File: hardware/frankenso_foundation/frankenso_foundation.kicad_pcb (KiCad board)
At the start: 2 copper layers, 5 parts, among them P99 0176122-06

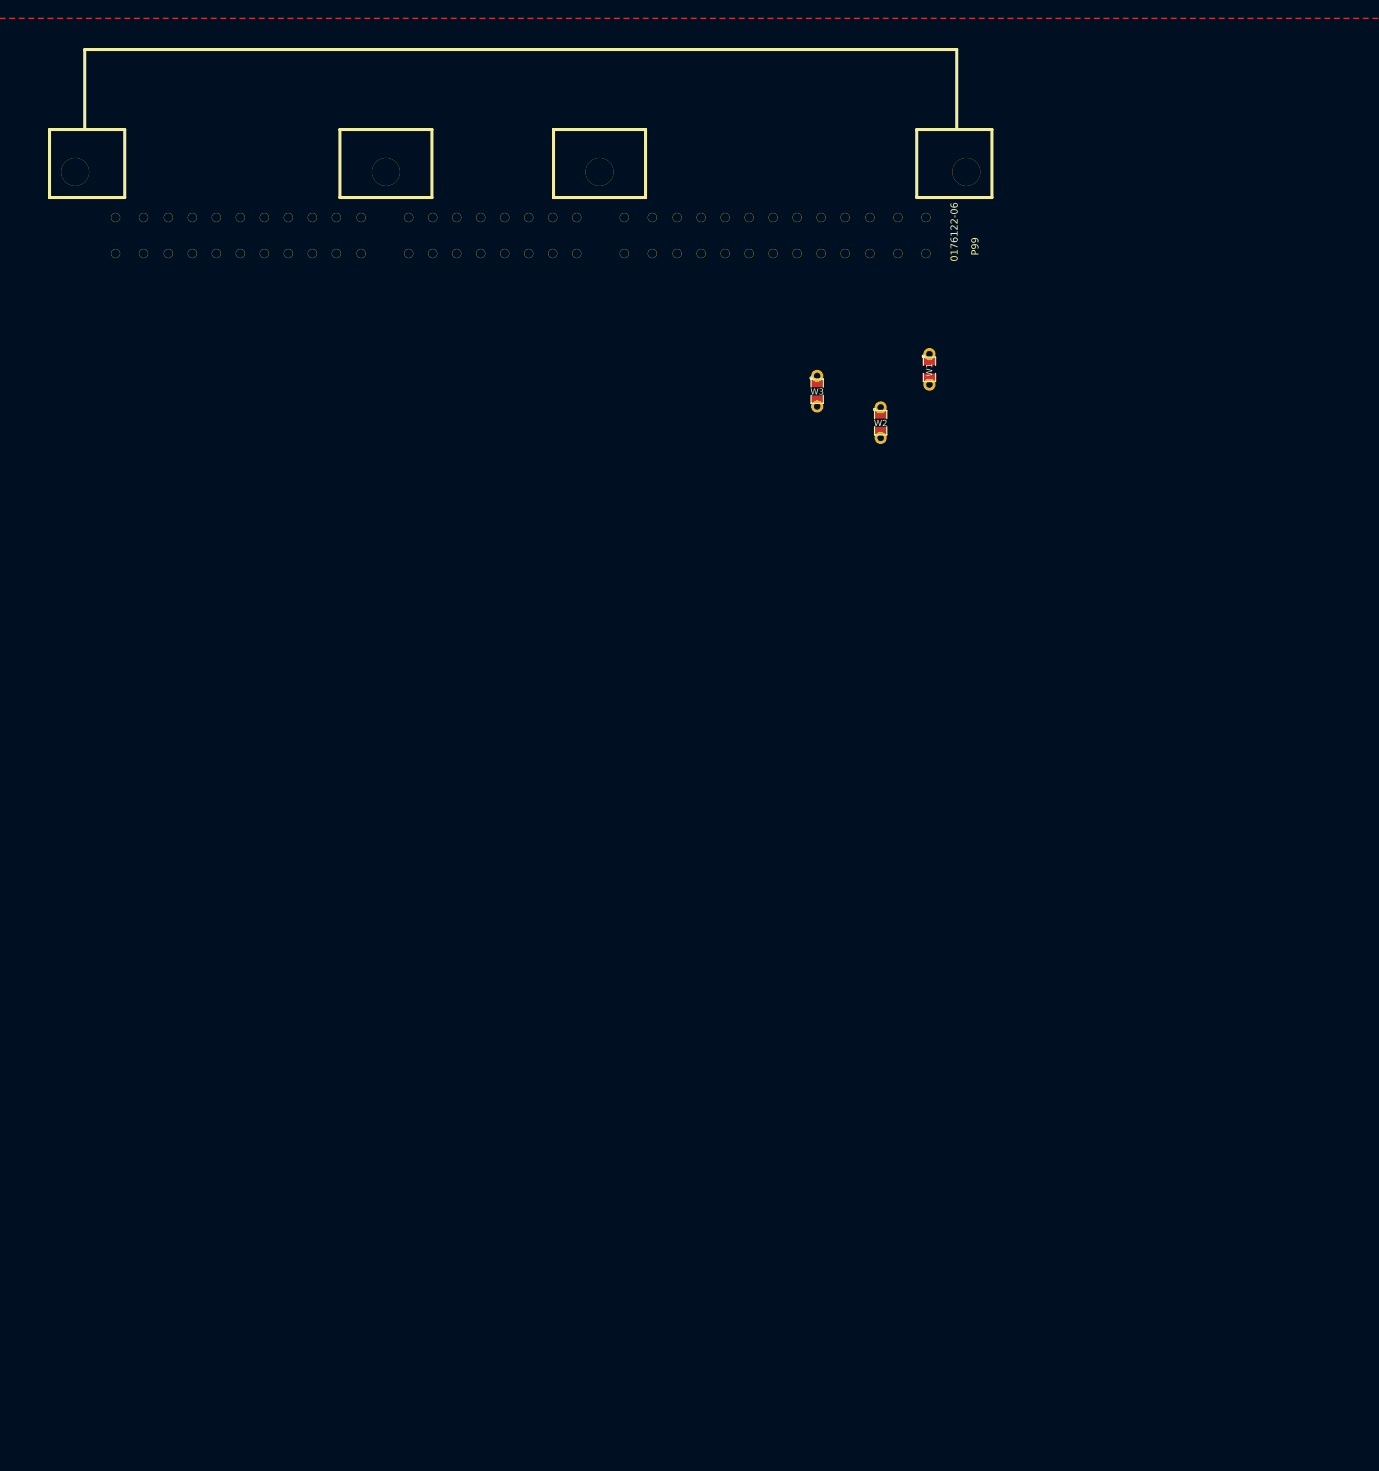
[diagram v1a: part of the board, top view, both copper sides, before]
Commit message: 
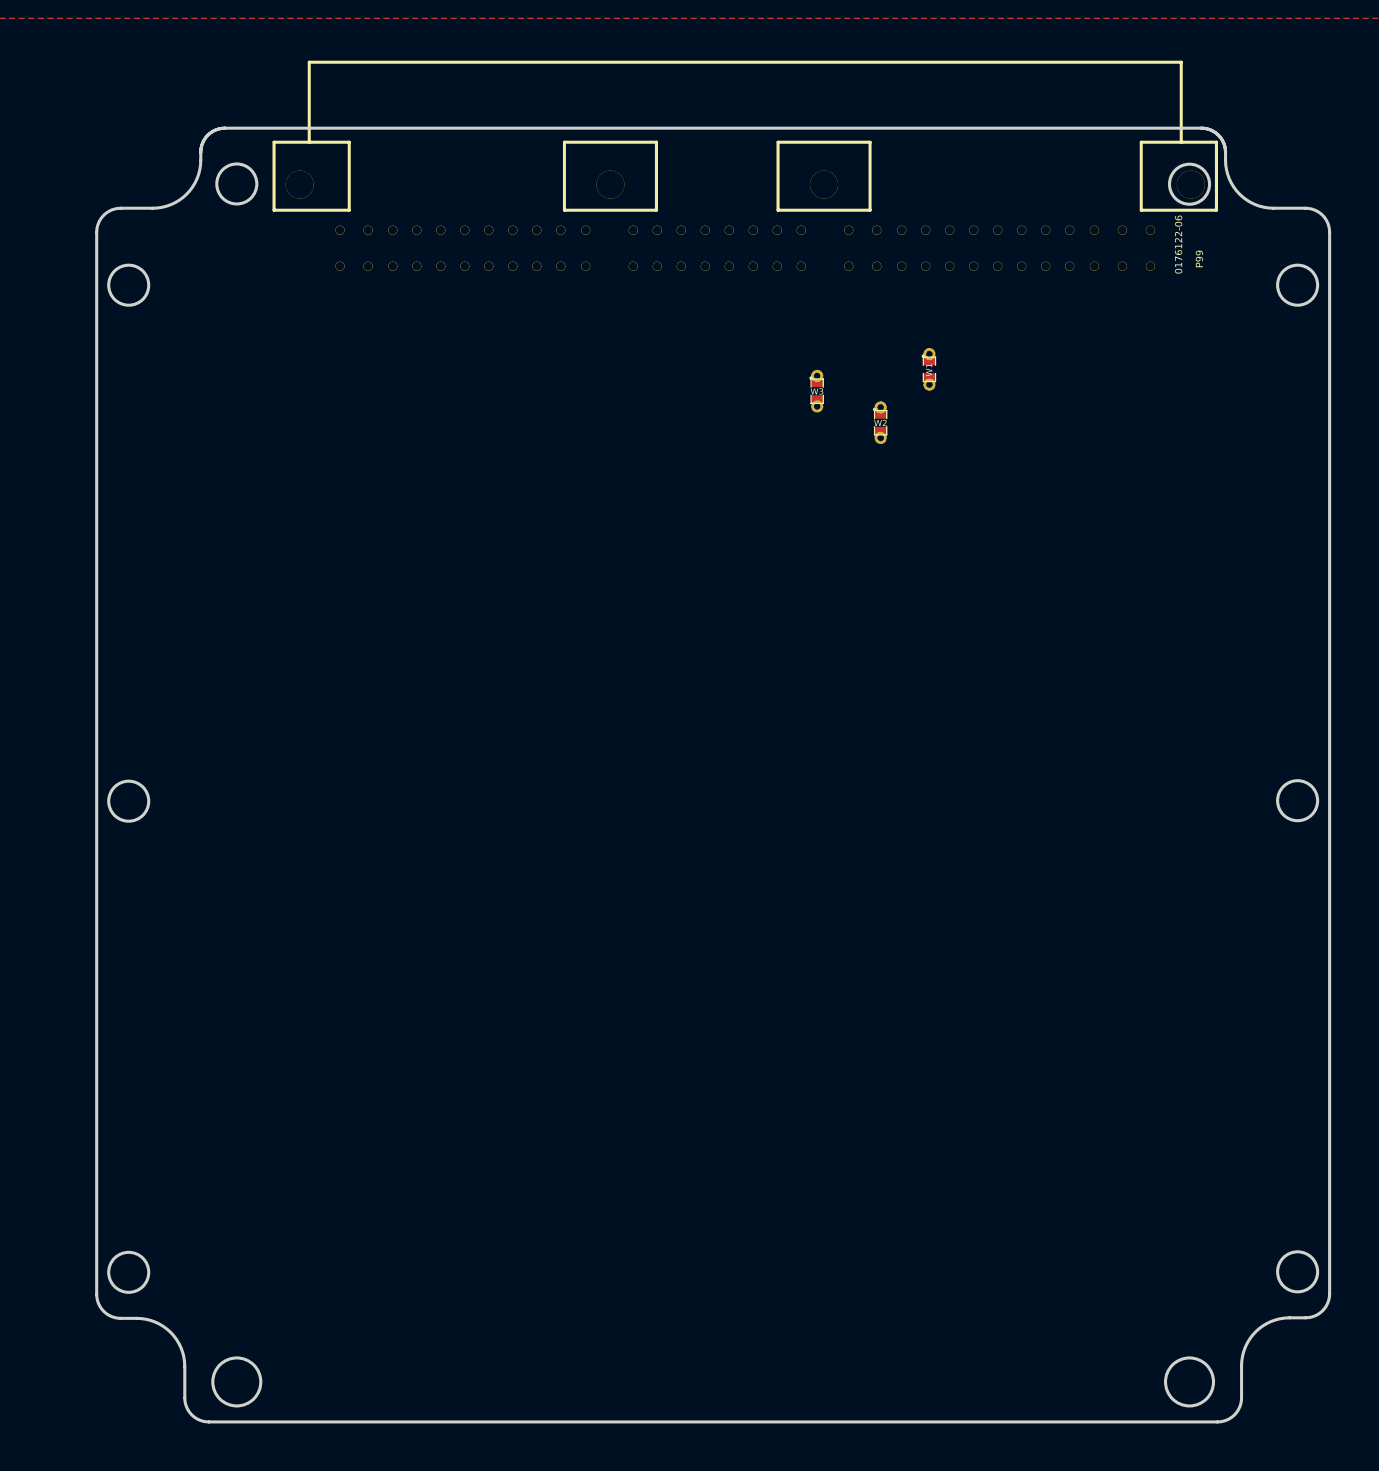
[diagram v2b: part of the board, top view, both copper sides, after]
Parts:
- moved P99 28.1 mm to (250.6, 110.0)
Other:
- board outline added: 154.1 x 161.7 mm
- net class Default: clearance 0.2032 -> 0.254
- rule pad_to_mask_clearance: 0 -> 0.2
- rule trace_clearance: 0.2032 -> 0.254
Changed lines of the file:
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@@
     (links 12)
     (no_connects 12)
-    (area 0 0 0 0)
+    (area 92 76 293.000001 271.000001)
     (thickness 1.6)
-    (drawings 13)
+    (drawings 49)
     (tracks 0)
     (zones 0)
@@
   (setup
     (last_trace_width 0.254)
-    (trace_clearance 0.2032)
-    (zone_clearance 0.254)
+    (trace_clearance 0.254)
+    (zone_clearance 0.381)
     (zone_45_only no)
     (trace_min 0.254)
-    (segment_width 0.2)
-    (edge_width 0.1)
+    (segment_width 0.3)
+    (edge_width 0.381)
     (via_size 0.889)
     (via_drill 0.635)
@@
     (uvia_min_size 0.508)
     (uvia_min_drill 0.127)
-    (pcb_text_width 0.3)
-    (pcb_text_size 1.5 1.5)
-    (mod_edge_width 0.15)
-    (mod_text_size 1 1)
-    (mod_text_width 0.15)
+    (pcb_text_width 0.3048)
+    (pcb_text_size 1.524 2.032)
+    (mod_edge_width 0.381)
+    (mod_text_size 1.524 1.524)
+    (mod_text_width 0.3048)
     (pad_size 1.524 1.524)
-    (pad_drill 1.016)
-    (pad_to_mask_clearance 0)
+    (pad_drill 0.508)
+    (pad_to_mask_clearance 0.2)
     (aux_axis_origin 0 0)
-    (visible_elements 7FFFFFBF)
+    (visible_elements 7FFFFFFF)
     (pcbplotparams
-      (layerselection 318537729)
+      (layerselection 3178497)
       (usegerberextensions true)
       (excludeedgelayer true)
-      (linewidth 0.150000)
+      (linewidth 0.100000)
       (plotframeref false)
       (viasonmask false)
@@
       (outputformat 1)
       (mirror false)
-      (drillshape 0)
+      (drillshape 1)
       (scaleselection 1)
-      (outputdirectory gerber))
+      (outputdirectory ""))
   )
   (net 0 "")
@@
   (net 5 N-000003)
   (net 6 N-000004)
-  (net_class Default "This is the default net class."
-    (clearance 0.2032)
+  (net_class Default "Это класс цепей по умолчанию."
+    (clearance 0.254)
     (trace_width 0.254)
     (via_dia 0.889)
@@
   )
   (module 176122-6 (layer F.Cu)
-    (at 222.504 108.3945)
+    (at 250.571 109.982)
     (fp_text reference P99 (at -2.10058 -0.89916 270) (layer F.SilkS)
       (effects (font (size 0.889 0.889) (thickness 0.22352)))
@@
   (gr_line (start 127 238.76) (end 129.54 238.76) (angle 90) (layer Cmts.User) (width 0.2))
   (gr_line (start 127 177.8) (end 127 238.76) (angle 90) (layer Cmts.User) (width 0.2))
+  (gr_circle (center 260.714 112.35478) (end 260.714 114.85668) (layer Edge.Cuts) (width 0.381))
+  (gr_circle (center 114.60304 112.35478) (end 114.60304 114.85668) (layer Edge.Cuts) (width 0.381))
+  (gr_arc (start 248.70488 95.72972) (end 251.70716 95.72972) (angle -90) (layer Edge.Cuts) (width 0.381))
+  (gr_circle (center 247.20374 249.44772) (end 247.20374 252.44772) (layer Edge.Cuts) (width 0.381))
+  (gr_arc (start 126.61216 95.72972) (end 126.61216 92.72744) (angle -90) (layer Edge.Cuts) (width 0.381))
+  (gr_circle (center 128.1133 249.44772) (end 128.1133 252.44772) (layer Edge.Cuts) (width 0.381))
+  (gr_line (start 250.70488 254.44772) (end 124.61216 254.44772) (angle 90) (layer Edge.Cuts) (width 0.381))
+  (gr_circle (center 247.20374 99.73276) (end 247.20374 102.23466) (layer Edge.Cuts) (width 0.381))
+  (gr_circle (center 128.1133 99.70228) (end 128.1133 102.20418) (layer Edge.Cuts) (width 0.381))
+  (gr_circle (center 260.714 176.79128) (end 260.714 179.29318) (layer Edge.Cuts) (width 0.381))
+  (gr_circle (center 260.714 235.68404) (end 260.714 238.18594) (layer Edge.Cuts) (width 0.381))
+  (gr_circle (center 114.60304 176.85478) (end 114.60304 179.35668) (layer Edge.Cuts) (width 0.381))
+  (gr_circle (center 114.60304 235.74754) (end 114.60304 238.24944) (layer Edge.Cuts) (width 0.381))
+  (gr_line (start 123.60988 95.72972) (end 123.60988 96.73048) (angle 90) (layer Edge.Cuts) (width 0.381))
+  (gr_line (start 117.60532 102.73504) (end 113.60228 102.73504) (angle 90) (layer Edge.Cuts) (width 0.381))
+  (gr_arc (start 117.60532 96.73048) (end 117.60532 102.73504) (angle -90) (layer Edge.Cuts) (width 0.381))
+  (gr_line (start 126.61216 92.72744) (end 248.70488 92.72744) (angle 90) (layer Edge.Cuts) (width 0.381))
+  (gr_line (start 251.70716 95.72972) (end 251.70716 96.73048) (angle 90) (layer Edge.Cuts) (width 0.381))
+  (gr_line (start 257.71172 102.73504) (end 261.71476 102.73504) (angle 90) (layer Edge.Cuts) (width 0.381))
+  (gr_arc (start 257.71172 96.73048) (end 251.70716 96.73048) (angle -90) (layer Edge.Cuts) (width 0.381))
+  (gr_arc (start 248.70488 95.72972) (end 251.70716 95.72972) (angle -90) (layer Edge.Cuts) (width 0.381))
+  (gr_arc (start 126.61216 95.72972) (end 126.61216 92.72744) (angle -90) (layer Edge.Cuts) (width 0.381))
+  (gr_line (start 253.70716 251.44544) (end 253.70716 247.43732) (angle 90) (layer Edge.Cuts) (width 0.381))
+  (gr_line (start 259.71172 241.43276) (end 261.71476 241.43276) (angle 90) (layer Edge.Cuts) (width 0.381))
+  (gr_line (start 115.60532 241.50134) (end 113.60228 241.50134) (angle 90) (layer Edge.Cuts) (width 0.381))
+  (gr_arc (start 259.71172 247.43732) (end 259.71172 241.43276) (angle -90) (layer Edge.Cuts) (width 0.381))
+  (gr_arc (start 115.60532 247.5059) (end 121.60988 247.5059) (angle -90) (layer Edge.Cuts) (width 0.381))
+  (gr_line (start 121.60988 247.5059) (end 121.60988 251.44544) (angle 90) (layer Edge.Cuts) (width 0.381))
+  (gr_line (start 110.6 105.73732) (end 110.6 238.49906) (angle 90) (layer Edge.Cuts) (width 0.381))
+  (gr_line (start 264.71704 105.73732) (end 264.71704 238.43048) (angle 90) (layer Edge.Cuts) (width 0.381))
+  (gr_arc (start 261.71476 105.73732) (end 264.71704 105.73732) (angle -89.9) (layer Edge.Cuts) (width 0.381))
+  (gr_arc (start 261.71476 238.43048) (end 261.71476 241.43276) (angle -90) (layer Edge.Cuts) (width 0.381))
+  (gr_arc (start 250.70488 251.44544) (end 250.70488 254.44772) (angle -90) (layer Edge.Cuts) (width 0.381))
+  (gr_arc (start 124.61216 251.44544) (end 121.60988 251.44544) (angle -90) (layer Edge.Cuts) (width 0.381))
+  (gr_arc (start 113.60228 238.49906) (end 110.6 238.49906) (angle -89.9) (layer Edge.Cuts) (width 0.381))
+  (gr_arc (start 113.60228 105.73732) (end 113.60228 102.73504) (angle -90) (layer Edge.Cuts) (width 0.381))
   (zone (net -1) (net_name GND) (layer F.Cu) (hatch edge 0.508)
     (connect_pads (clearance 0.254))

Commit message: frankenso foundation progress
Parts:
- removed P_VOID3: CONN_8, pin_array_8x2
- added W10: TEST, SM0805_jumper, F.Cu at (151.8, 64.8)
- added W11: TEST, SM0805_jumper, F.Cu at (156.8, 71.1)
- added W12: TEST, SM0805_jumper, F.Cu at (154.9, 64.8)
- added W13: TEST, SM0805_jumper, F.Cu at (160.0, 71.1)
- added W14: TEST, SM0805_jumper, F.Cu at (158.1, 64.8)
- added W15: TEST, SM0805_jumper, F.Cu at (163.2, 71.1)
- added W16: TEST, SM0805_jumper, F.Cu at (161.3, 64.8)
- added W17: TEST, SM0805_jumper, F.Cu at (166.4, 71.1)
- added W18: TEST, SM0805_jumper, F.Cu at (164.5, 64.8)
- added W19: TEST, SM0805_jumper, F.Cu at (169.5, 71.1)
- added W20: TEST, SM0805_jumper, F.Cu at (167.6, 64.8)
- added W21: TEST, SM0805_jumper, F.Cu at (172.7, 71.1)
- added W22: TEST, SM0805_jumper, F.Cu at (170.8, 64.8)
- added W23: TEST, SM0805_jumper, F.Cu at (177.8, 71.1)
- added W24: TEST, SM0805_jumper, F.Cu at (175.9, 64.8)
- added W25: TEST, SM0805_jumper, F.Cu at (181.0, 71.1)
- added W26: TEST, SM0805_jumper, F.Cu at (179.1, 64.8)
- added W27: TEST, SM0805_jumper, F.Cu at (184.2, 71.1)
- added W28: TEST, SM0805_jumper, F.Cu at (182.2, 64.8)
- added W29: TEST, SM0805_jumper, F.Cu at (187.3, 71.1)
- added W30: TEST, SM0805_jumper, F.Cu at (185.4, 64.8)
- added W31: TEST, SM0805_jumper, F.Cu at (190.5, 71.1)
- added W32: TEST, SM0805_jumper, F.Cu at (188.6, 64.8)
- added W33: TEST, SM0805_jumper, F.Cu at (193.7, 71.1)
- added W34: TEST, SM0805_jumper, F.Cu at (191.8, 64.8)
- added W35: TEST, SM0805_jumper, F.Cu at (196.8, 71.1)
- added W36: TEST, SM0805_jumper, F.Cu at (194.9, 64.8)
- added W37: TEST, SM0805_jumper, F.Cu at (200.0, 71.1)
- added W38: TEST, SM0805_jumper, F.Cu at (198.1, 64.8)
- added W39: TEST, SM0805_jumper, F.Cu at (205.1, 71.1)
- added W4: TEST, SM0805_jumper, F.Cu at (142.2, 64.8)
- added W40: TEST, SM0805_jumper, F.Cu at (203.2, 64.8)
- added W41: TEST, SM0805_jumper, F.Cu at (208.3, 71.1)
- added W42: TEST, SM0805_jumper, F.Cu at (206.4, 64.8)
- added W43: TEST, SM0805_jumper, F.Cu at (211.5, 71.1)
- added W44: TEST, SM0805_jumper, F.Cu at (209.6, 64.8)
- added W45: TEST, SM0805_jumper, F.Cu at (214.6, 71.1)
- added W46: TEST, SM0805_jumper, F.Cu at (212.7, 64.8)
- added W47: TEST, SM0805_jumper, F.Cu at (217.8, 71.1)
- added W48: TEST, SM0805_jumper, F.Cu at (215.9, 64.8)
- added W49: TEST, SM0805_jumper, F.Cu at (221.0, 71.1)
- added W5: TEST, SM0805_jumper, F.Cu at (147.3, 71.1)
- added W50: TEST, SM0805_jumper, F.Cu at (219.1, 64.8)
- added W51: TEST, SM0805_jumper, F.Cu at (224.2, 71.1)
- added W52: TEST, SM0805_jumper, F.Cu at (222.2, 64.8)
- added W53: TEST, SM0805_jumper, F.Cu at (227.3, 71.1)
- added W54: TEST, SM0805_jumper, F.Cu at (225.4, 64.8)
- added W55: TEST, SM0805_jumper, F.Cu at (230.5, 71.1)
- added W56: TEST, SM0805_jumper, F.Cu at (228.6, 64.8)
- added W57: TEST, SM0805_jumper, F.Cu at (233.7, 71.1)
- added W58: TEST, SM0805_jumper, F.Cu at (231.8, 64.8)
- added W59: TEST, SM0805_jumper, F.Cu at (236.9, 71.1)
- added W6: TEST, SM0805_jumper, F.Cu at (145.4, 64.8)
- added W60: TEST, SM0805_jumper, F.Cu at (234.9, 64.8)
- added W61: TEST, SM0805_jumper, F.Cu at (240.0, 71.1)
- added W62: TEST, SM0805_jumper, F.Cu at (238.1, 64.8)
- added W63: TEST, SM0805_jumper, F.Cu at (243.2, 71.1)
- added W64: TEST, SM0805_jumper, F.Cu at (241.3, 64.8)
- added W7: TEST, SM0805_jumper, F.Cu at (150.5, 71.1)
- added W8: TEST, SM0805_jumper, F.Cu at (148.6, 64.8)
- added W9: TEST, SM0805_jumper, F.Cu at (153.7, 71.1)
- P99: value 0176122-06 -> 176122-6_2ND; footprint 176122-6 -> 176122-6_2nd
- moved W2 95.0 mm to (139.1, 64.8), turned to 90 degrees
- moved W1 90.1 mm to (141.0, 71.1), turned to 90 degrees
- moved W3 78.5 mm to (144.1, 71.1), turned to 90 degrees
- moved P99 50.5 mm to (250.8, 59.4)
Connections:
- P99 pad 1: N-000003 -> N-00000104
- P99 pad 10: (no net) -> N-00000108
- P99 pad 11: (no net) -> N-0000083
- P99 pad 12: (no net) -> N-00000102
- P99 pad 13: (no net) -> N-0000098
- P99 pad 14: (no net) -> N-0000094
- P99 pad 15: (no net) -> N-0000090
- P99 pad 16: (no net) -> N-0000086
- P99 pad 17: (no net) -> N-00000121
- P99 pad 18: (no net) -> N-00000117
- P99 pad 19: (no net) -> N-00000114
- P99 pad 2: N-000004 -> N-00000100
- P99 pad 20: (no net) -> N-00000110
- P99 pad 21: (no net) -> N-00000106
- P99 pad 22: (no net) -> N-0000081
- P99 pad 23: (no net) -> N-0000051
- P99 pad 24: (no net) -> N-0000049
- P99 pad 25: (no net) -> N-0000044
- P99 pad 26: (no net) -> N-0000040
- P99 pad 27: (no net) -> N-0000036
- P99 pad 28: (no net) -> N-0000032
- P99 pad 29: (no net) -> N-0000028
- P99 pad 3: N-000002 -> N-0000096
- P99 pad 30: (no net) -> N-0000046
- P99 pad 31: (no net) -> N-0000050
- P99 pad 32: (no net) -> N-0000048
- P99 pad 33: (no net) -> N-0000042
- P99 pad 34: (no net) -> N-0000038
- P99 pad 35: (no net) -> N-0000034
- P99 pad 36: (no net) -> N-0000030
- P99 pad 37: (no net) -> N-0000026
- P99 pad 38: (no net) -> N-0000045
- P99 pad 39: (no net) -> N-000003
- P99 pad 4: (no net) -> N-0000092
- P99 pad 40: (no net) -> N-0000024
- P99 pad 41: (no net) -> N-0000020
- P99 pad 42: (no net) -> N-0000016
- P99 pad 43: (no net) -> N-0000013
- P99 pad 44: (no net) -> N-000009
- P99 pad 45: (no net) -> N-0000079
- P99 pad 46: (no net) -> N-0000075
- P99 pad 47: (no net) -> N-0000071
- P99 pad 48: (no net) -> N-0000068
- P99 pad 49: (no net) -> N-0000059
- P99 pad 5: (no net) -> N-0000088
- P99 pad 50: (no net) -> N-0000058
- P99 pad 51: (no net) -> N-0000056
- P99 pad 52: (no net) -> N-000001
- P99 pad 53: (no net) -> N-0000022
- P99 pad 54: (no net) -> N-0000018
- P99 pad 55: (no net) -> N-0000015
- P99 pad 56: (no net) -> N-0000011
- P99 pad 57: (no net) -> N-000007
- P99 pad 58: (no net) -> N-0000077
- P99 pad 59: (no net) -> N-0000073
- P99 pad 6: (no net) -> N-00000123
- P99 pad 60: (no net) -> N-0000070
- P99 pad 61: (no net) -> N-0000066
- P99 pad 62: (no net) -> N-0000053
- P99 pad 63: (no net) -> N-0000057
- P99 pad 64: (no net) -> N-0000055
- P99 pad 7: (no net) -> N-00000119
- P99 pad 8: (no net) -> N-00000115
- P99 pad 9: (no net) -> N-00000112
- W1 pad 1: N-000003 -> (no net)
- W1 pad 2: /INJ-12 -> N-00000104
- W2 pad 1: N-000004 -> (no net)
- W2 pad 2: /INJ-11 -> N-00000102
- W3 pad 1: N-000002 -> (no net)
- W3 pad 2: /INJ-10 -> N-00000100
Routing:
- net (no net): track 0.00 -> 4.55 mm
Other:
- outline, holes or cut-outs redrawn

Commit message: making progress with the PCB
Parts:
- added S?: DISPLAY, DISPLAY_4x20, F.Cu at (193.7, 187.3)
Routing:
- net N-0000059: track 0.00 -> 21.0 mm
- net N-00000100: track 0.00 -> 20.9 mm
- net N-0000058: track 0.00 -> 20.7 mm
- net N-00000104: track 0.00 -> 20.6 mm
- net N-0000024: track 0.00 -> 20.5 mm
- net N-0000083: track 0.00 -> 20.2 mm
- net N-0000056: track 0.00 -> 20.1 mm
- net N-000003: track 0.00 -> 19.8 mm
- net N-0000098: track 0.00 -> 18.0 mm
- net N-0000057: track 0.00 -> 17.9 mm
- net N-0000053: track 0.00 -> 17.9 mm
- net N-00000102: track 0.00 -> 17.7 mm
- net N-0000055: track 0.00 -> 17.5 mm
- net N-0000022: track 0.00 -> 17.5 mm
- net N-0000081: track 0.00 -> 17.4 mm
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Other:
- outline, holes or cut-outs redrawn
- net class 1A external added: clearance 0.2159, trace_width 0.3048, via_dia 0.6858, via_drill 0.3302
- net class 2.5A external added: clearance 0.2159, trace_width 1.0668, via_dia 0.6858, via_drill 0.3302
- net class 5A external added: clearance 0.2159, trace_width 2.7178, via_dia 1.54178, via_drill 1.18618
- net class Default: clearance 0.254 -> 0.2159; trace_width 0.254 -> 0.2159; via_dia 0.889 -> 0.6858; via_drill 0.635 -> 0.3302
- net class min2_extern_.188A added: clearance 0.1524, trace_width 0.1524, via_dia 0.6858, via_drill 0.3302
- net class min_extern_.241A added: clearance 0.2159, trace_width 0.2159, via_dia 0.6858, via_drill 0.3302
- rule trace_clearance: 0.254 -> 0.2159
- rule trace_min: 0.254 -> 0.1524
- rule via_min_drill: 0.508 -> 0.3302
- rule via_min_size: 0.889 -> 0

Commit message: pinout
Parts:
- removed S?: DISPLAY, DISPLAY_4x20
- added S1: DISPLAY_BL, DISPLAY_4x20_BL, F.Cu at (193.7, 187.2)
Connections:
- W55 pad 1: (no net) -> /CLT
- W57 pad 1: (no net) -> /INJ-02
- W58 pad 1: (no net) -> /INJ-03
- W59 pad 1: (no net) -> /INJ-04
- W60 pad 1: (no net) -> /INJ-05
- W61 pad 1: (no net) -> /IDL-SPEED-SOL
- W62 pad 1: (no net) -> /INJ-07
- W63 pad 1: (no net) -> /3Y
- W64 pad 1: (no net) -> /3Z
